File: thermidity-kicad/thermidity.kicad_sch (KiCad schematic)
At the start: 13 parts, among them J1 Battery, J2 Display, J3 ISP, U1 ATmega328P, U2 HIH-5030, U3 TMP36

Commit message: Ratiometric measurement of temperature with a thermistor (#18)
- replace TMP36 with a thermistor NTC 100k
- put back 1nF cap between AREF and GND
- wait 150us for the cap to discharge before converting with 1.1V reference
- uint16_t is enough for 16x ADC
- SMD footprint instead of TH for thermistor
- calculate temperature
- rounding of temperature compensated relative humidity
- no need for battery voltage in mV
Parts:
- removed C3: 100nF, Capacitor_SMD:C_1206_3216Metric_Pad1.33x1.80mm_HandSolder, symbol Device:C
- removed U3: TMP36, TMP36GT9:XDCR_TMP36GT9, symbol TMP36GT9:TMP36GT9
- added C2: 1nF, Capacitor_SMD:C_1206_3216Metric_Pad1.33x1.80mm_HandSolder, symbol Device:C
- added R3: 100k, Resistor_SMD:R_0805_2012Metric_Pad1.20x1.40mm_HandSolder, symbol Device:R
- added TH1: NTC 100k, Resistor_SMD:R_0805_2012Metric_Pad1.20x1.40mm_HandSolder, symbol Device:Thermistor_NTC
- R1: value 1M -> 300K
- R2: value 1M -> 1.2M
- renumbered C2 to C3, R3 to R4
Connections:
- net GND: now also C2.1, R3.2
- net at R2.1, U1.24 (PC1), U2.3 (+VE): now also TH1.1
- net at U1.20 (AREF): now also C2.2
- net at U1.25 (PC2): now also R3.1, TH1.2

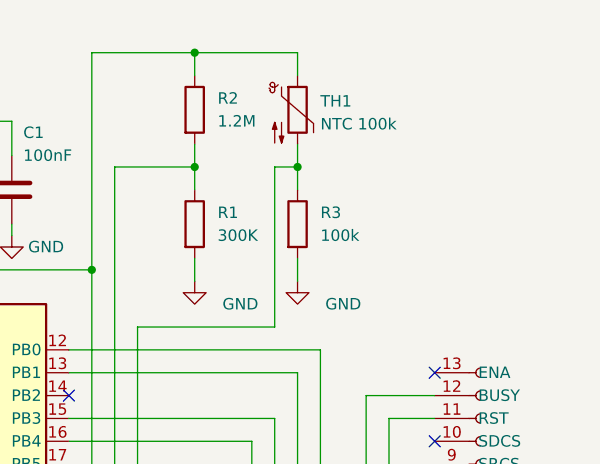
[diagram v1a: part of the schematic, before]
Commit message: update README and schematic + PCB
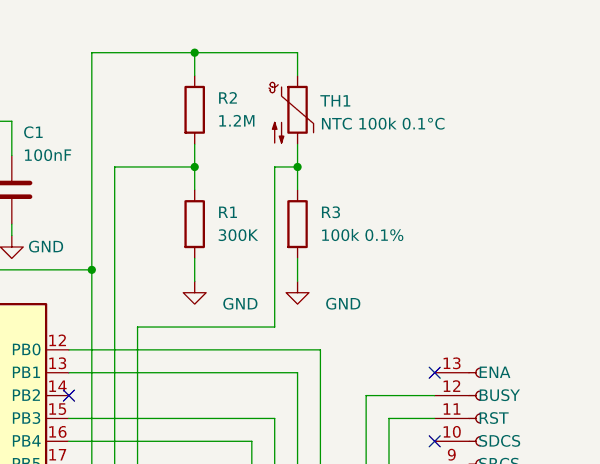
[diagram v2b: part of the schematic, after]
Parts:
- R3: value 100k -> 100k 0.1%
- TH1: value NTC 100k -> NTC 100k 0.1°C
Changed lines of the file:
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@@
       (effects (font (size 1.27 1.27)) (justify left))
     )
-    (property "Value" "100k" (id 1) (at 189.23 53.3399 0)
+    (property "Value" "100k 0.1%" (id 1) (at 189.23 53.3399 0)
       (effects (font (size 1.27 1.27)) (justify left))
     )
@@
       (effects (font (size 1.27 1.27)) (justify left))
     )
-    (property "Value" "NTC 100k" (id 1) (at 189.23 40.9574 0)
+    (property "Value" "NTC 100k 0.1°C" (id 1) (at 189.23 40.9574 0)
       (effects (font (size 1.27 1.27)) (justify left))
     )
@@
     )
     (path "/67107e66-dfe9-4c53-82c3-246c71b667ae"
-      (reference "R3") (unit 1) (value "100k") (footprint "Resistor_SMD:R_0805_2012Metric_Pad1.20x1.40mm_HandSolder")
+      (reference "R3") (unit 1) (value "100k 0.1%") (footprint "Resistor_SMD:R_0805_2012Metric_Pad1.20x1.40mm_HandSolder")
     )
     (path "/ce63e81c-5d78-4d98-bb9e-4b0f5b9f1c49"
@@
     )
     (path "/982b487a-58ee-40be-91ad-fe1876106c60"
-      (reference "TH1") (unit 1) (value "NTC 100k") (footprint "Resistor_SMD:R_0805_2012Metric_Pad1.20x1.40mm_HandSolder")
+      (reference "TH1") (unit 1) (value "NTC 100k 0.1°C") (footprint "Resistor_SMD:R_0805_2012Metric_Pad1.20x1.40mm_HandSolder")
     )
     (path "/a564f624-0149-43d3-9b25-20abc178b1e7"
